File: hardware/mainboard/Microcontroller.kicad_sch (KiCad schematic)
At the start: 19 parts

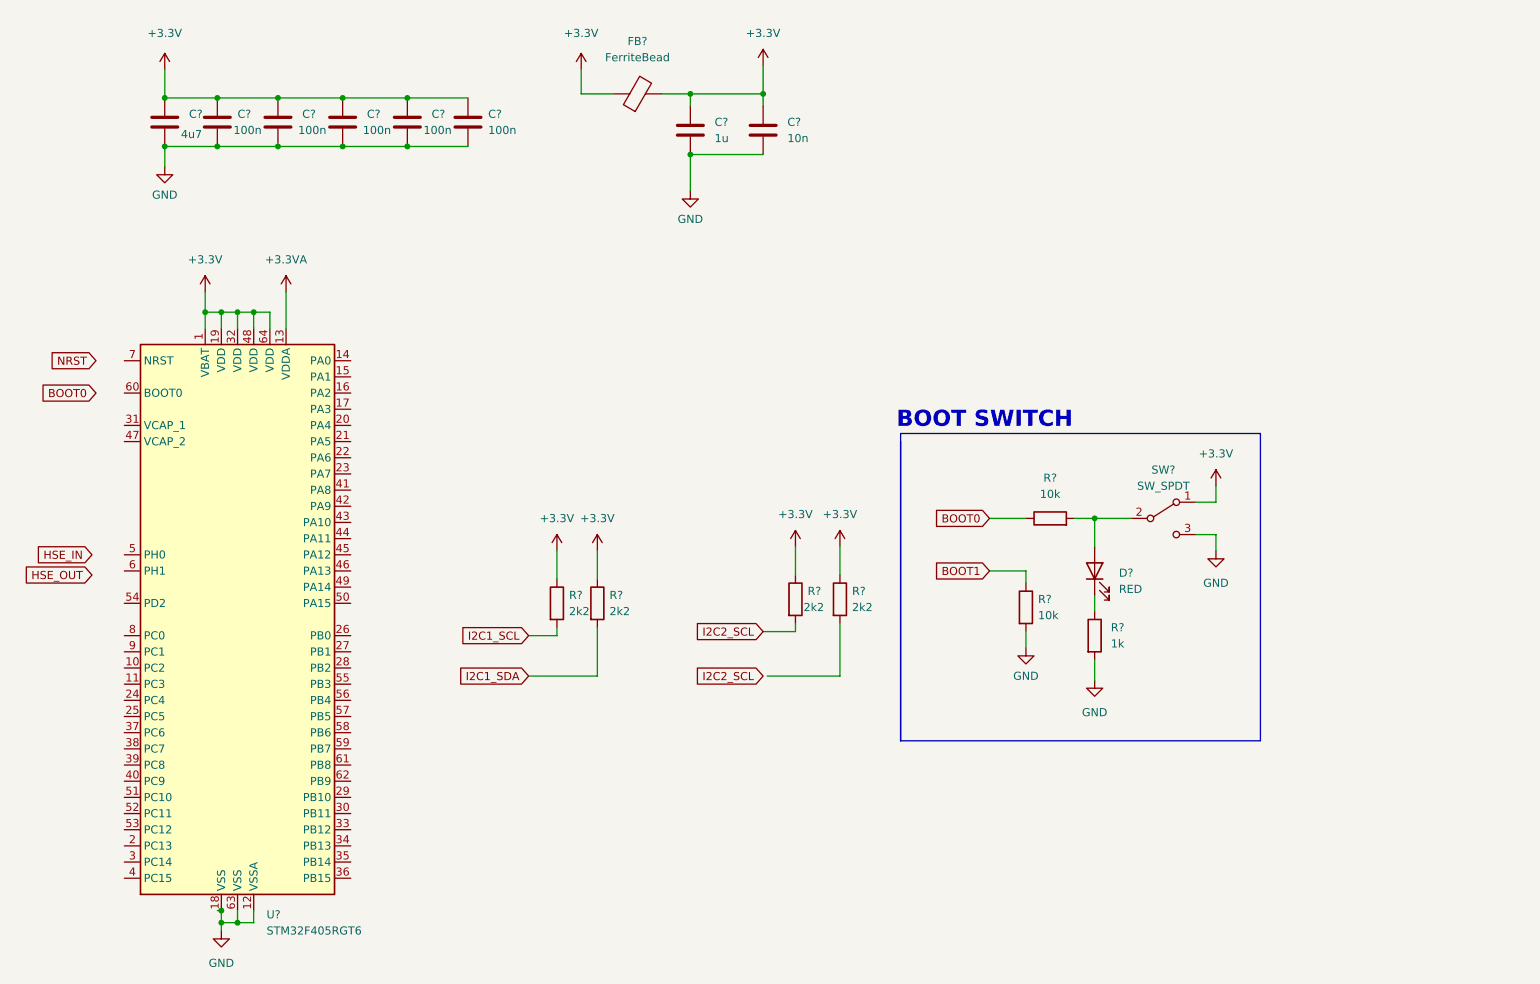
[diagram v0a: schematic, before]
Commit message: Added Jy-901 Bluetooth and Wifi
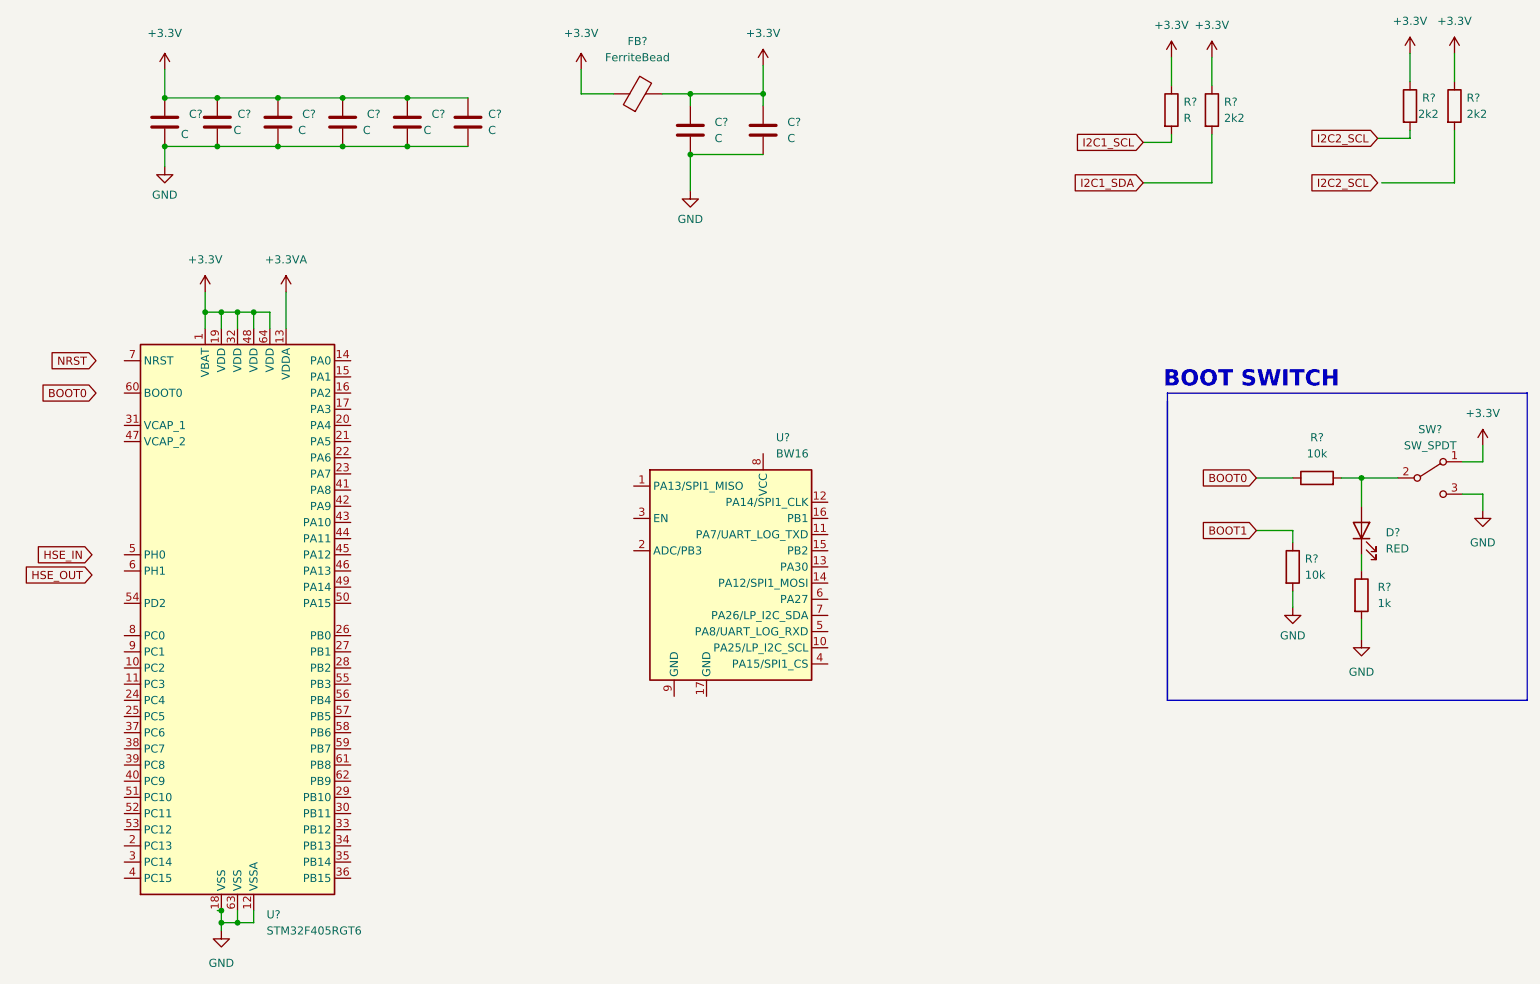
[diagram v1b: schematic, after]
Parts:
- added U?: BW16, BW16 RF module, symbol sensors:BW16
- C?: value 4u7 -> C
- C? (x5): value 100n -> C
- C?: value 1u -> C
- C?: value 10n -> C
- R?: value 2k2 -> R
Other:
- moved on the sheet: D?, R?, SW?
